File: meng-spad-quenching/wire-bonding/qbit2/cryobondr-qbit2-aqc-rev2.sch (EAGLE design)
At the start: 13 parts, among them IC1 QBIT2-WIREBOND-CRYO1, X1 CONN-D3, X2 CONN-D5, X3 CONN-D4, X4 CONN-D2, X5 CONN-D1, X6 CONN-D6, X7 CONN-D7, X8 CONN-D8

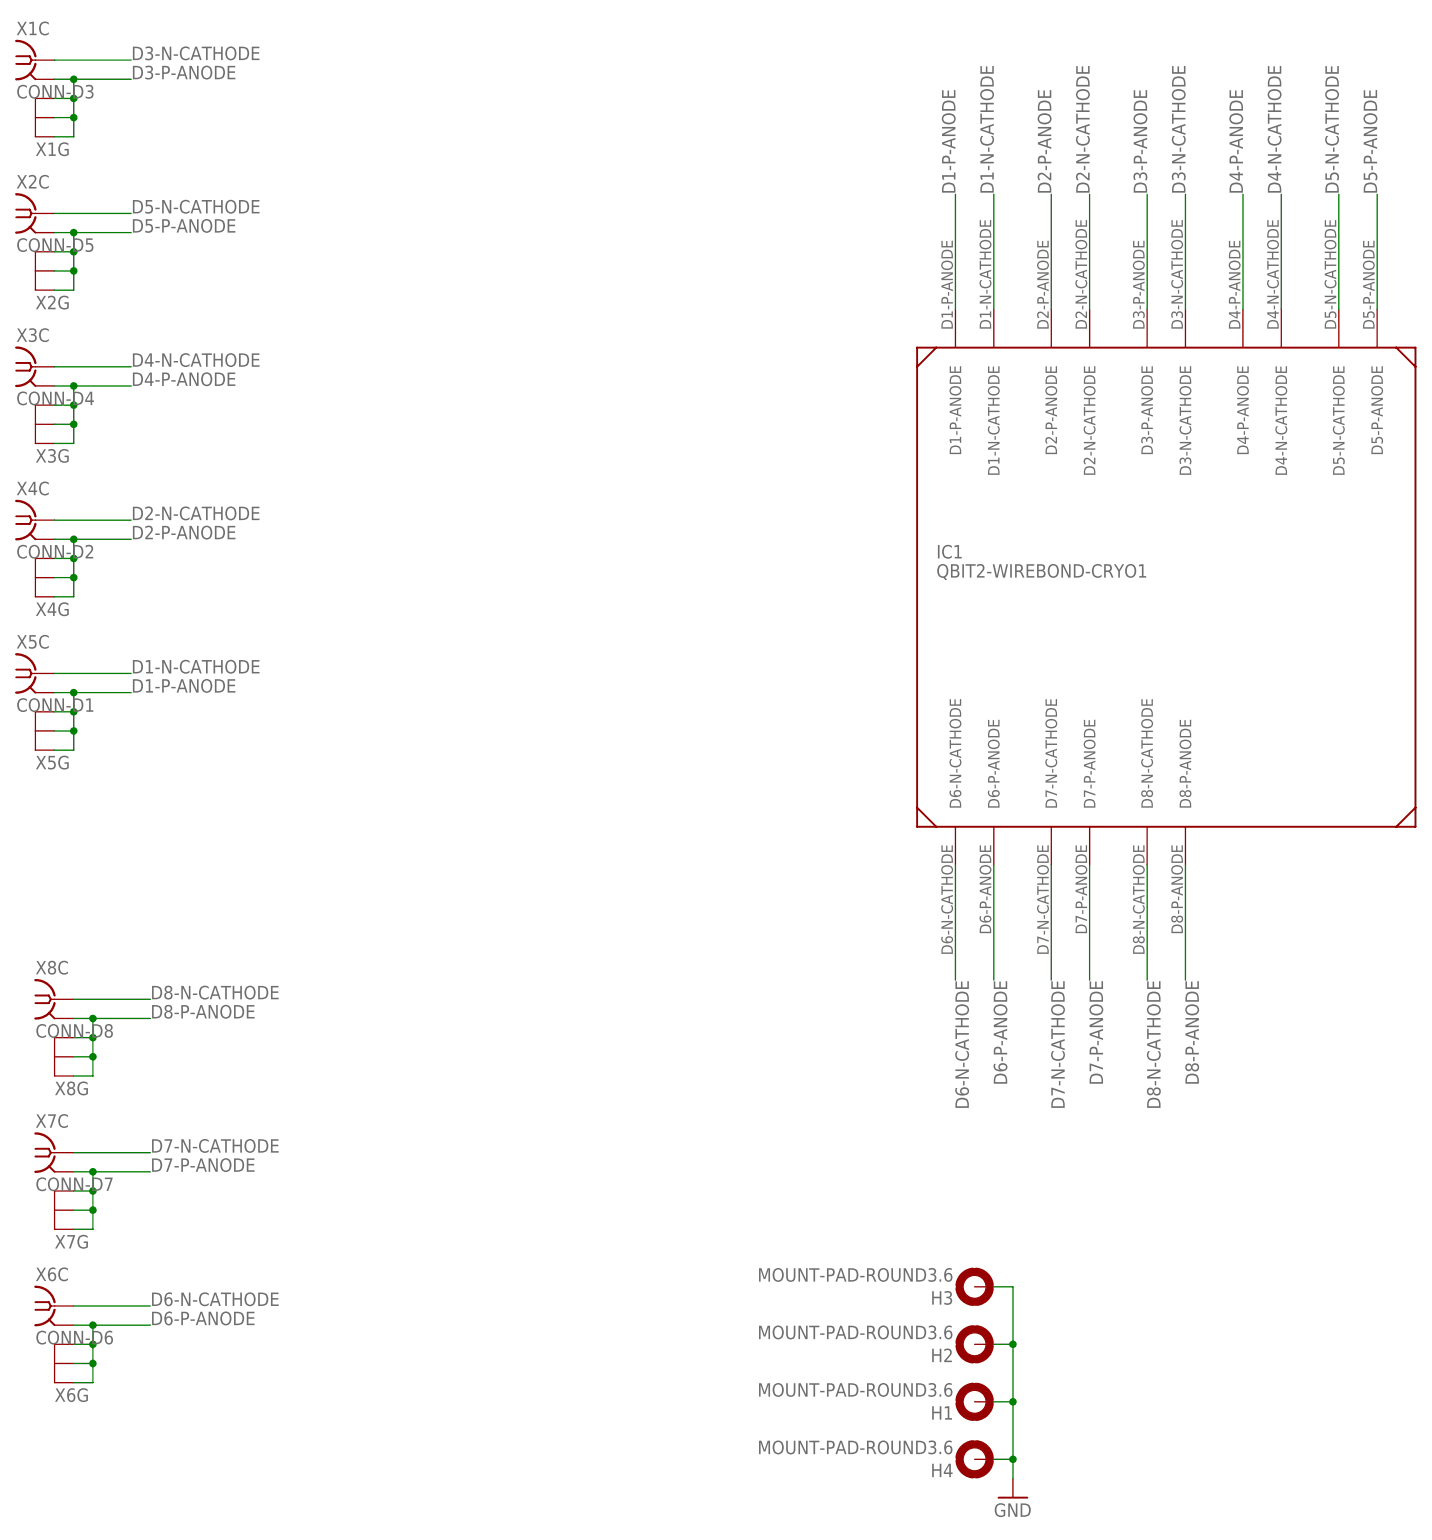
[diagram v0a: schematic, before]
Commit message: Added TVS diodes to all SPADs, grounded all anodes
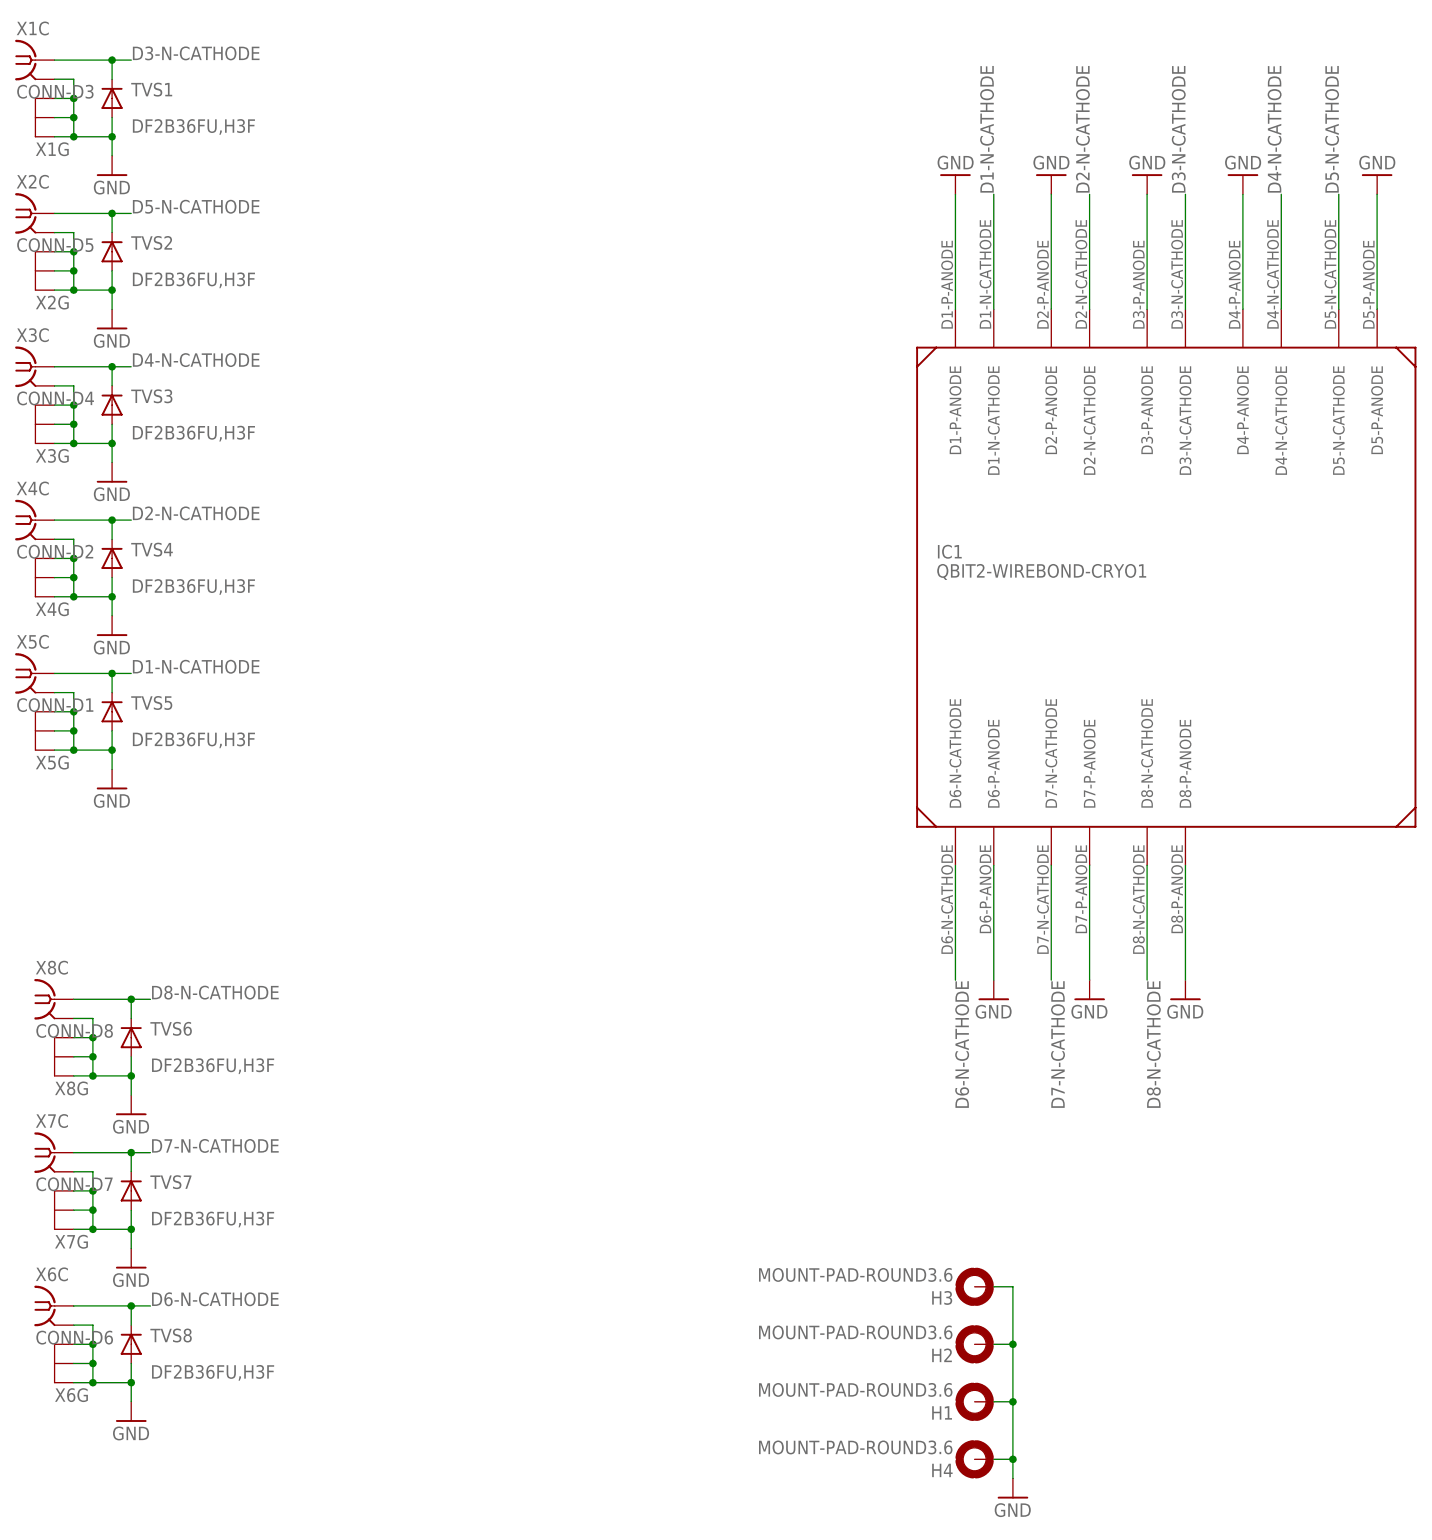
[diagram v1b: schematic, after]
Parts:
- added TVS1, TVS2, TVS3, TVS4, TVS5, TVS6, TVS7, TVS8: DF2B36FU,H3F, diode:DIODE-SOD323-W
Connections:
- removed net D1-P-ANODE: IC1.D1-P-ANODE, X5C.GND, X5G.GND@1, X5G.GND@2, X5G.GND@3
- removed net D2-P-ANODE: IC1.D2-P-ANODE, X4C.GND, X4G.GND@1, X4G.GND@2, X4G.GND@3
- removed net D3-P-ANODE: IC1.D3-P-ANODE, X1C.GND, X1G.GND@1, X1G.GND@2, X1G.GND@3
- removed net D4-P-ANODE: IC1.D4-P-ANODE, X3C.GND, X3G.GND@1, X3G.GND@2, X3G.GND@3
- removed net D5-P-ANODE: IC1.D5-P-ANODE, X2C.GND, X2G.GND@1, X2G.GND@2, X2G.GND@3
- removed net D6-P-ANODE: IC1.D6-P-ANODE, X6C.GND, X6G.GND@1, X6G.GND@2, X6G.GND@3
- removed net D7-P-ANODE: IC1.D7-P-ANODE, X7C.GND, X7G.GND@1, X7G.GND@2, X7G.GND@3
- removed net D8-P-ANODE: IC1.D8-P-ANODE, X8C.GND, X8G.GND@1, X8G.GND@2, X8G.GND@3
- net D1-N-CATHODE: now also TVS5.C
- net D2-N-CATHODE: now also TVS4.C
- net D3-N-CATHODE: now also TVS1.C
- net D4-N-CATHODE: now also TVS3.C
- net D5-N-CATHODE: now also TVS2.C
- net D6-N-CATHODE: now also TVS8.C
- net D7-N-CATHODE: now also TVS7.C
- net D8-N-CATHODE: now also TVS6.C
- net GND: now also IC1.D1-P-ANODE, IC1.D2-P-ANODE, IC1.D3-P-ANODE, IC1.D4-P-ANODE, IC1.D5-P-ANODE, IC1.D6-P-ANODE, IC1.D7-P-ANODE, IC1.D8-P-ANODE, TVS1.A, TVS2.A, TVS3.A, TVS4.A, TVS5.A, TVS6.A, TVS7.A, TVS8.A, X1C.GND, X1G.GND@1, X1G.GND@2, X1G.GND@3, X2C.GND, X2G.GND@1, X2G.GND@2, X2G.GND@3, X3C.GND, X3G.GND@1, X3G.GND@2, X3G.GND@3, X4C.GND, X4G.GND@1, X4G.GND@2, X4G.GND@3, X5C.GND, X5G.GND@1, X5G.GND@2, X5G.GND@3, X6C.GND, X6G.GND@1, X6G.GND@2, X6G.GND@3, X7C.GND, X7G.GND@1, X7G.GND@2, X7G.GND@3, X8C.GND, X8G.GND@1, X8G.GND@2, X8G.GND@3

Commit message: work on wirebonding board
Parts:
- IC1: value QBIT2-WIREBOND-CRYO1 -> QBIT2-WIREBOND-CRYO2; device meng:QBIT2-WIREBOND-CRYO1 -> meng:QBIT2-WIREBOND-CRYO2
- TVS1, TVS2, TVS3, TVS4, TVS5, TVS7, TVS8: device diode:DIODE-SOD323-W -> diode:DIODE-SOD323-R
- X1: value CONN-D3 -> CONN-D1
- X2: value CONN-D5 -> CONN-D2
- X3: value CONN-D4 -> CONN-D3
- X4: value CONN-D2 -> CONN-D4
- X5: value CONN-D1 -> CONN-D5
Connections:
- net D1-N-CATHODE: now also TVS1.C, X1C.1; no longer TVS5.C, X5C.1
- net D2-N-CATHODE: now also TVS2.C, X2C.1; no longer TVS4.C, X4C.1
- net D3-N-CATHODE: now also TVS3.C, X3C.1; no longer TVS1.C, X1C.1
- net D4-N-CATHODE: now also TVS4.C, X4C.1; no longer TVS3.C, X3C.1
- net D5-N-CATHODE: now also TVS5.C, X5C.1; no longer TVS2.C, X2C.1
- net D6-N-CATHODE: now also TVS6.C; no longer TVS8.C
- net D8-N-CATHODE: now also TVS8.C; no longer TVS6.C
- net GND: now also IC1.VSS_BOTTOM, IC1.VSS_TOP
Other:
- moved on the sheet: TVS1, TVS2, TVS3, TVS4, TVS5, TVS6, TVS8, X1C, X1G, X2C, X2G, X3C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

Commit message: Added plotter to leaf heater system class
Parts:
- TVS6: device diode:DIODE-SOD323-W -> diode:DIODE-SOD323-R
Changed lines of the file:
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@@
 <part name="TVS8" library="diode" library_urn="urn:adsk.eagle:library:210" deviceset="DIODE-" device="SOD323-R" package3d_urn="urn:adsk.eagle:package:43437/1" value="DF2B36FU,H3F"/>
 <part name="TVS7" library="diode" library_urn="urn:adsk.eagle:library:210" deviceset="DIODE-" device="SOD323-R" package3d_urn="urn:adsk.eagle:package:43437/1" value="DF2B36FU,H3F"/>
-<part name="TVS6" library="diode" library_urn="urn:adsk.eagle:library:210" deviceset="DIODE-" device="SOD323-W" package3d_urn="urn:adsk.eagle:package:43418/1" value="DF2B36FU,H3F"/>
+<part name="TVS6" library="diode" library_urn="urn:adsk.eagle:library:210" deviceset="DIODE-" device="SOD323-R" package3d_urn="urn:adsk.eagle:package:43437/1" value="DF2B36FU,H3F"/>
 <part name="GND8" library="supply1" deviceset="GND" device=""/>
 <part name="GND9" library="supply1" deviceset="GND" device=""/>
